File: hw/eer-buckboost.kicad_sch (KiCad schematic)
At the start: 60 parts, among them IC7702 LTC3779IFE#PBF, Q7701 BSC360N15NS3 G, Q7702 BSC360N15NS3 G, Q7703 BSC360N15NS3 G, Q7704 BSC360N15NS3 G, U7751 TLV9062xD, U7752 NVTFS6H888NLTAG, U7753 PCT2075DP

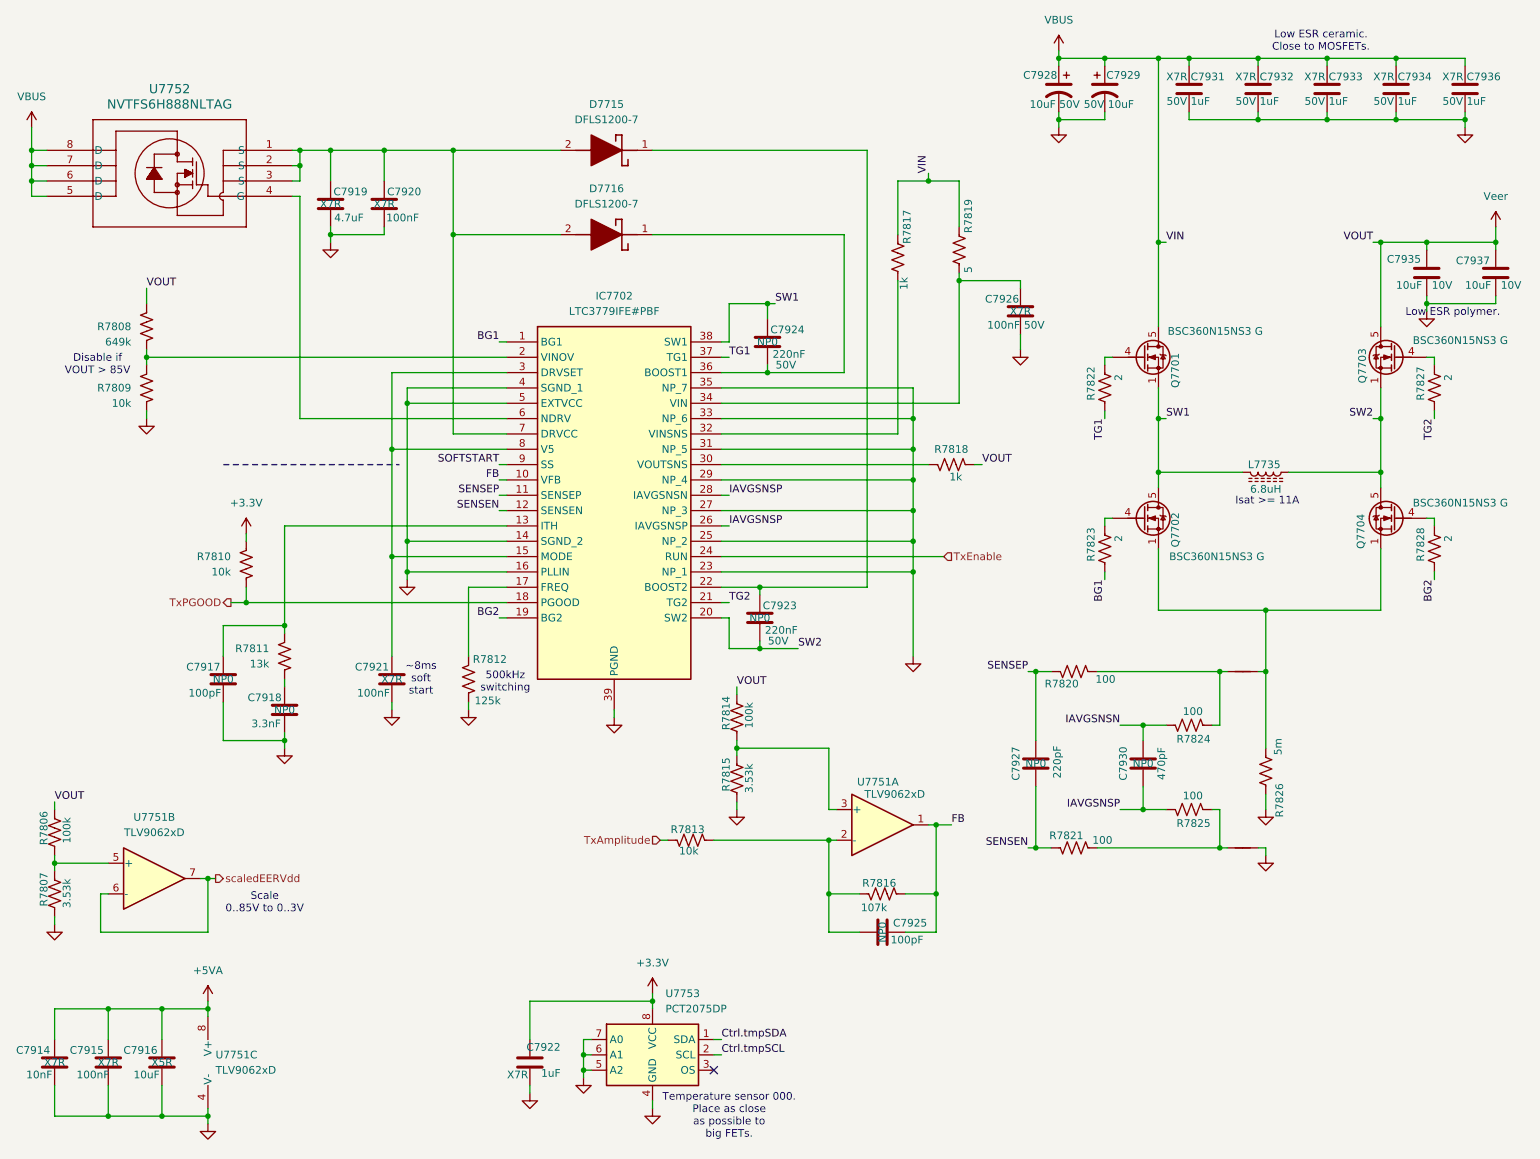
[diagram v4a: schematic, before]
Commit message: Starting to build guanella transformers. Mostly converted to 1-2-1 tx, but FPGA still to do.
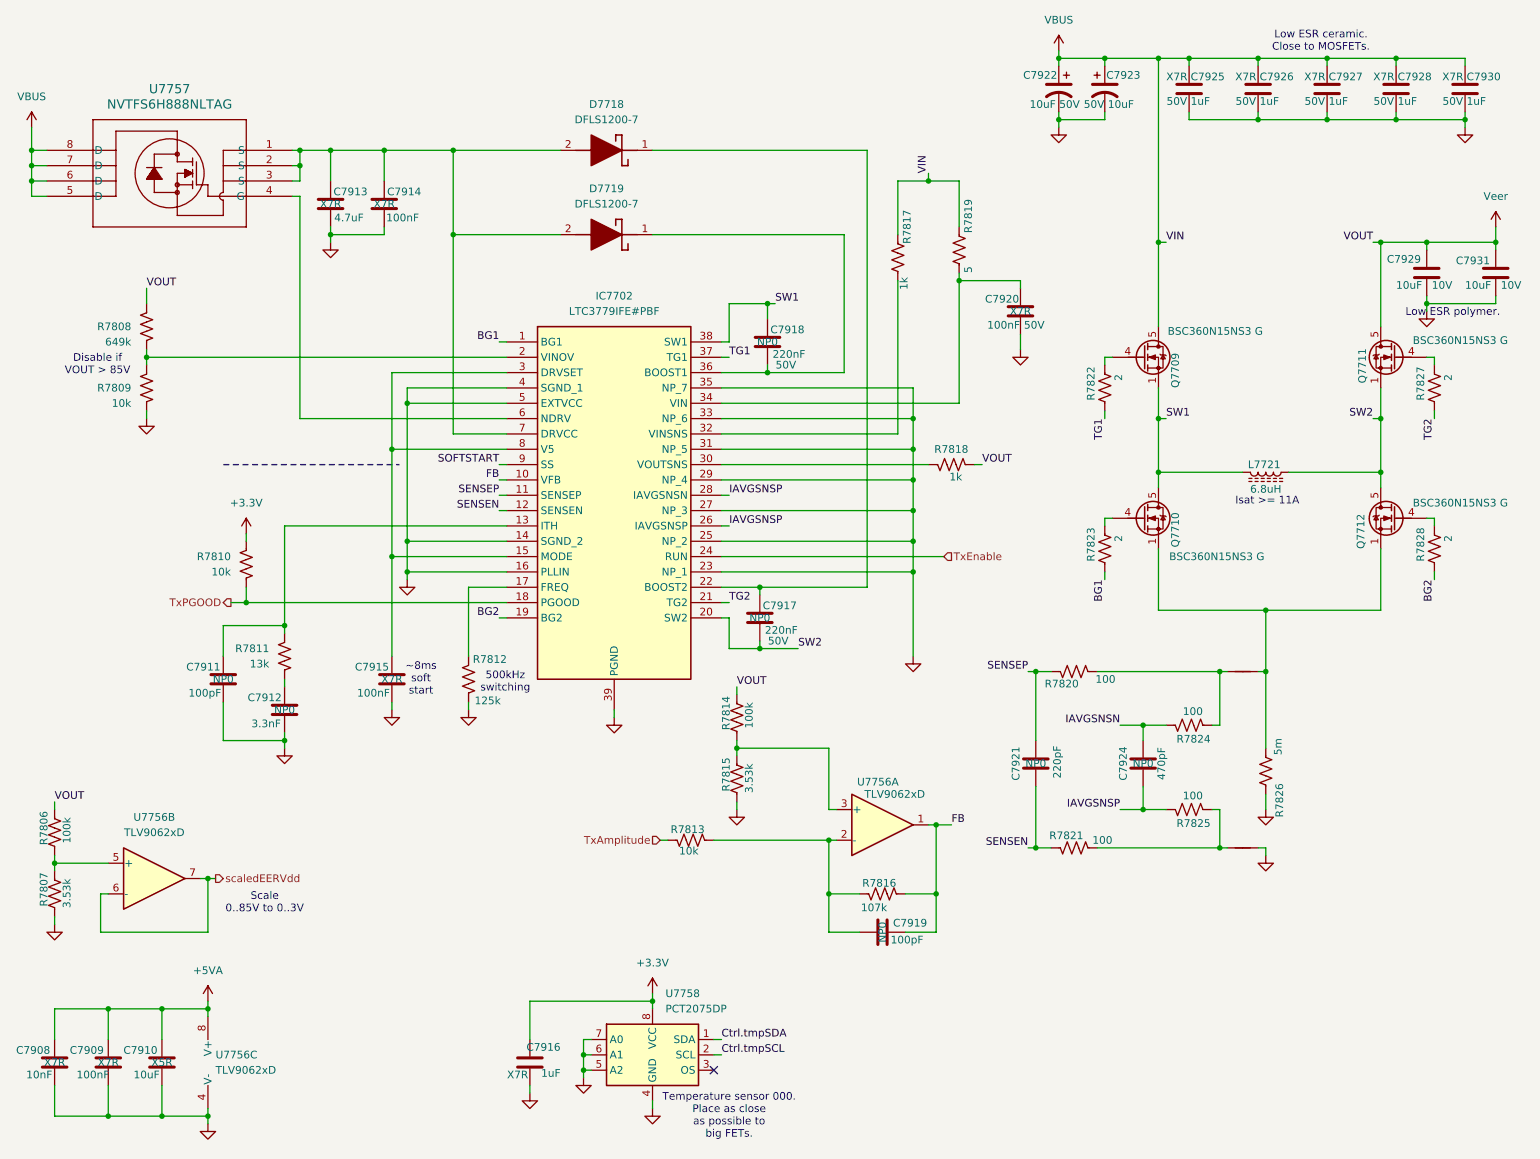
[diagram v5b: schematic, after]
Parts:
- renumbered C7914 to C7908, C7915 to C7909, C7916 to C7910, C7917 to C7911, C7918 to C7912, C7919 to C7913, C7920 to C7914, C7921 to C7915, C7922 to C7916, C7923 to C7917, C7924 to C7918, C7925 to C7919, C7926 to C7920, C7927 to C7921, C7928 to C7922, C7929 to C7923, C7930 to C7924, C7931 to C7925, C7932 to C7926, C7933 to C7927, C7934 to C7928, C7935 to C7929, C7936 to C7930, C7937 to C7931, D7715 to D7718, D7716 to D7719, L7735 to L7721, Q7701 to Q7709, Q7702 to Q7710, Q7703 to Q7711, Q7704 to Q7712, U7751 to U7756, U7752 to U7757, U7753 to U7758

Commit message: Checkpoint. FPGA is mostly done (need a check!). Working on new LPFs. Need inductor footprints and to fix a bunch of broken/missing footprints.
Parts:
- C7908, C7909, C7914, C7915, C7920: footprint Capacitor_SMD:C_0805_2012Metric -> Capacitor_SMD:C_0603_1608Metric
- C7911, C7912, C7919, C7921, C7924: footprint Capacitor_SMD:C_0201_0603Metric -> Capacitor_SMD:C_0603_1608Metric
- R7806, R7809, R7810, R7813, R7814: footprint Resistor_SMD:R_0603_1608Metric -> Resistor_SMD:R_0402_1005Metric
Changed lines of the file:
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@@
 			)
 		)
-		(property "Footprint" "Capacitor_SMD:C_0805_2012Metric"
+		(property "Footprint" "Capacitor_SMD:C_0603_1608Metric"
 			(at 75.2348 49.53 0)
 			(effects
@@
 			)
 		)
-		(property "Footprint" "Capacitor_SMD:C_0805_2012Metric"
+		(property "Footprint" "Capacitor_SMD:C_0603_1608Metric"
 			(at 182.5752 59.69 0)
 			(effects
@@
 			)
 		)
-		(property "Footprint" "Capacitor_SMD:C_0201_0603Metric"
+		(property "Footprint" "Capacitor_SMD:C_0603_1608Metric"
 			(at 50.4952 128.27 0)
 			(effects
@@
 			)
 		)
-		(property "Footprint" "Resistor_SMD:R_0603_1608Metric"
+		(property "Footprint" "Resistor_SMD:R_0402_1005Metric"
 			(at 133.604 130.556 90)
 			(effects
@@
 			)
 		)
-		(property "Footprint" "Resistor_SMD:R_0603_1608Metric"
+		(property "Footprint" "Resistor_SMD:R_0402_1005Metric"
 			(at 52.324 105.664 90)
 			(effects
@@
 			)
 		)
-		(property "Footprint" "Resistor_SMD:R_0603_1608Metric"
+		(property "Footprint" "Resistor_SMD:R_0402_1005Metric"
 			(at 35.814 76.454 90)
 			(effects
@@
 			)
 		)
-		(property "Footprint" "Resistor_SMD:R_0603_1608Metric"
+		(property "Footprint" "Resistor_SMD:R_0402_1005Metric"
 			(at 20.574 149.606 90)
 			(effects
@@
 			)
 		)
-		(property "Footprint" "Capacitor_SMD:C_0805_2012Metric"
+		(property "Footprint" "Capacitor_SMD:C_0603_1608Metric"
 			(at 22.5552 191.77 0)
 			(effects
@@
 			)
 		)
-		(property "Footprint" "Capacitor_SMD:C_0201_0603Metric"
+		(property "Footprint" "Capacitor_SMD:C_0603_1608Metric"
 			(at 60.6552 133.35 0)
 			(effects
@@
 			)
 		)
-		(property "Footprint" "Capacitor_SMD:C_0805_2012Metric"
+		(property "Footprint" "Capacitor_SMD:C_0603_1608Metric"
 			(at 31.4452 191.77 0)
 			(effects
@@
 			)
 		)
-		(property "Footprint" "Resistor_SMD:R_0603_1608Metric"
+		(property "Footprint" "Resistor_SMD:R_0402_1005Metric"
 			(at 127.254 152.146 90)
 			(effects
@@
 			)
 		)
-		(property "Footprint" "Capacitor_SMD:C_0201_0603Metric"
+		(property "Footprint" "Capacitor_SMD:C_0603_1608Metric"
 			(at 202.8952 134.62 0)
 			(effects
@@
 			)
 		)
-		(property "Footprint" "Capacitor_SMD:C_0201_0603Metric"
+		(property "Footprint" "Capacitor_SMD:C_0603_1608Metric"
 			(at 162.56 165.4048 0)
 			(effects
@@
 			)
 		)
-		(property "Footprint" "Capacitor_SMD:C_0201_0603Metric"
+		(property "Footprint" "Capacitor_SMD:C_0603_1608Metric"
 			(at 185.1152 134.62 0)
 			(effects
@@
 			)
 		)
-		(property "Footprint" "Capacitor_SMD:C_0805_2012Metric"
+		(property "Footprint" "Capacitor_SMD:C_0603_1608Metric"
 			(at 78.4352 128.27 0)
 			(effects

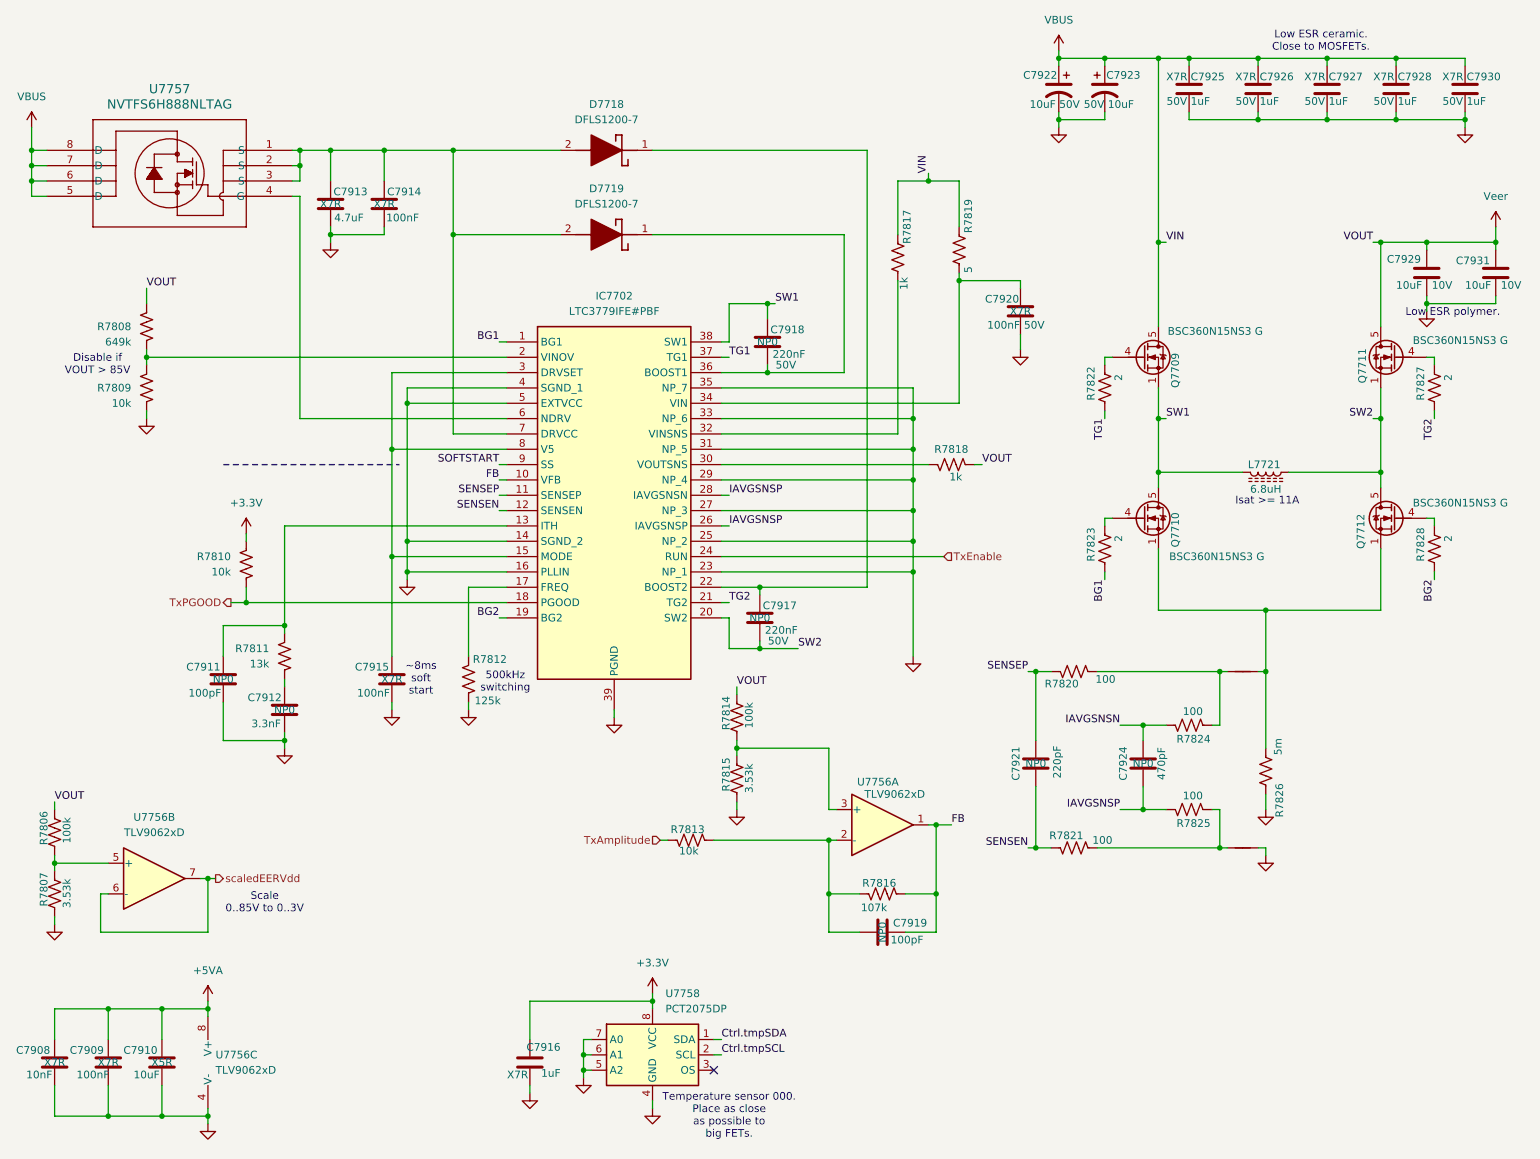
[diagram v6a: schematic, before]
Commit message: OK I have part numbers for consolidated caps, resistors, inductors and all ICs are now Uxxx refdes.
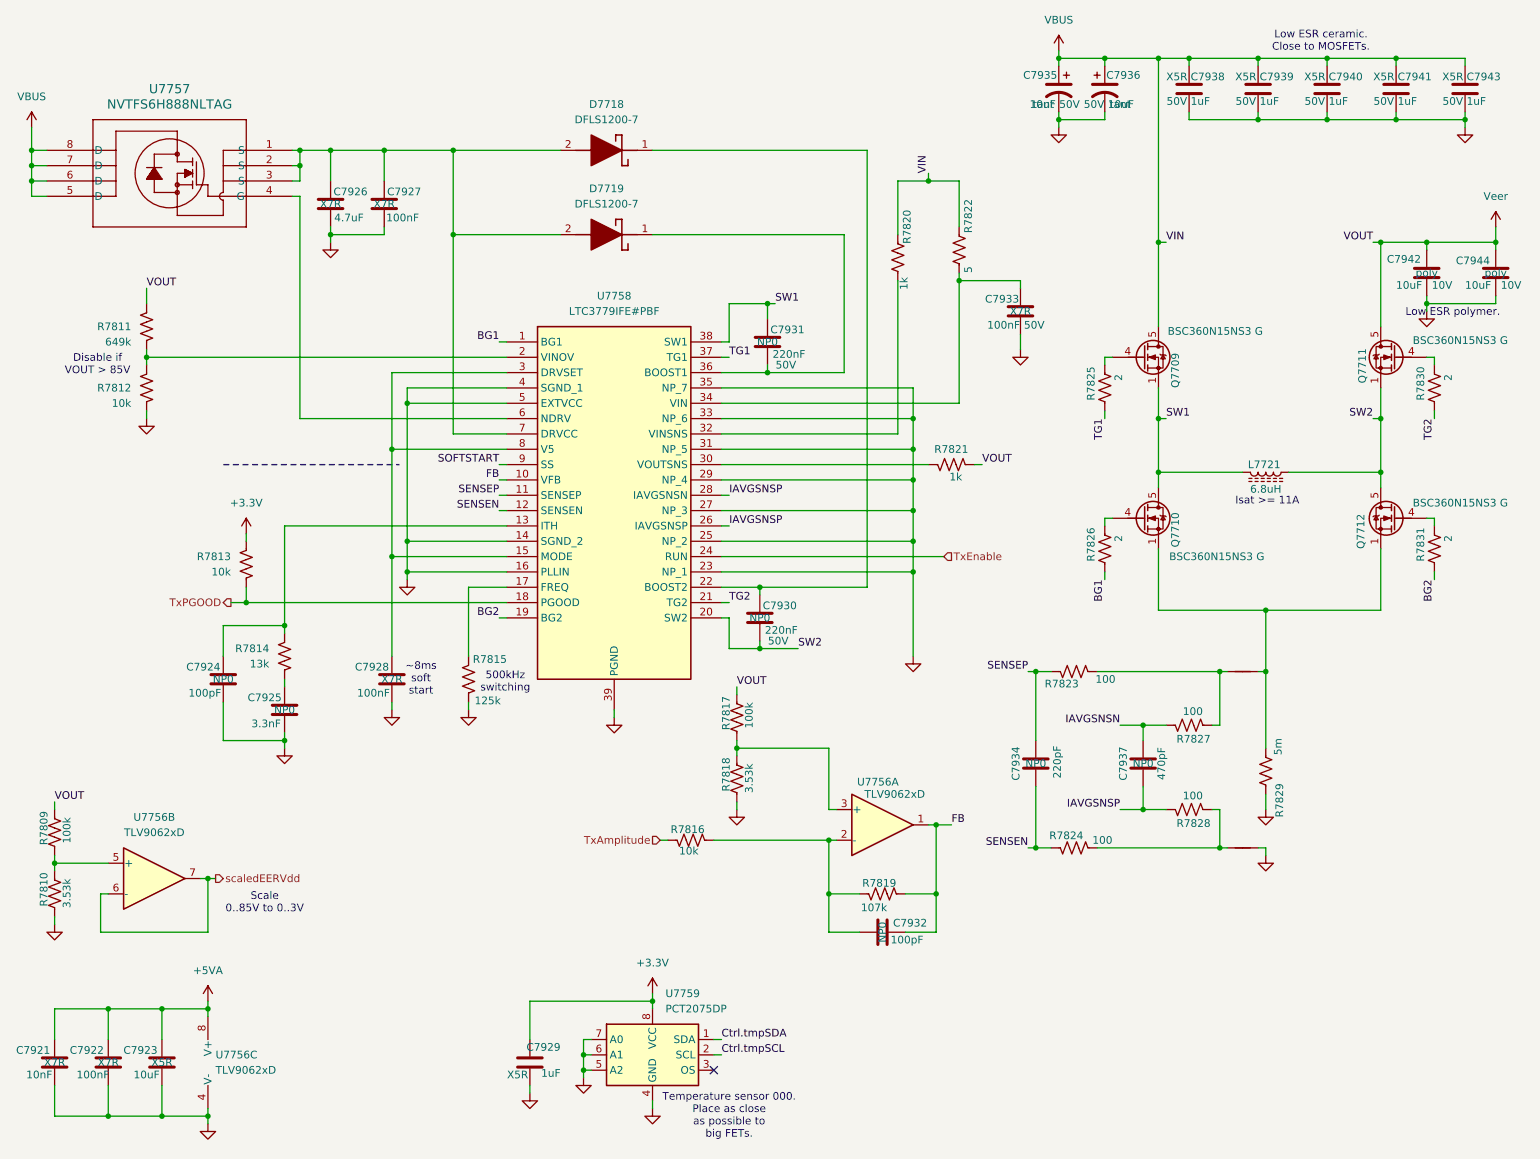
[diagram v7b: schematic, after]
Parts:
- C7921: renamed from C7908; Manufacturer_Name (none) -> Murata; Manufacturer_Part_Number (none) -> GCM1885C2A103JE02J; Mouser Part Number (none) -> 81-GCM1885C2A103JE2J
- C7922: renamed from C7909; Manufacturer_Name (none) -> Kemet; Manufacturer_Part_Number C0603X224J5RACTU -> C0805F104K1RACAUTO; Mouser Part Number 80-C0603X224J5RTU -> 80-C0805F104K1RAUTO
- C7923: renamed from C7910; footprint Capacitor_SMD:C_0805_2012Metric -> Capacitor_SMD:C_0603_1608Metric; Manufacturer_Name (none) -> Taoup Uidem; Manufacturer_Part_Number (none) -> 81-GXT155R71E223KE1D; Mouser Part Number (none) -> 963-MLAST168BB5106MT; working-voltage 10V -> 25V
- C7924: renamed from C7911; Manufacturer_Name (none) -> TDK; Manufacturer_Part_Number (none) -> CGA3E2C0G1H101J080AE; Mouser Part Number (none) -> 810-CGA3E2C0G1H101JA
- C7925: renamed from C7912; Manufacturer_Name (none) -> TDK; Manufacturer_Part_Number (none) -> C1608C0G1H332J080AE; Mouser Part Number (none) -> 810-C1608C0G1H332J08
- C7926: renamed from C7913; Manufacturer_Name (none) -> Kyocera AVX; Manufacturer_Part_Number (none) -> 08055D475KAT4A; Mouser Part Number (none) -> 581-08055D475KAT4A
- C7927: renamed from C7914; Manufacturer_Name (none) -> Kemet; Manufacturer_Part_Number C0603X224J5RACTU -> C0805F104K1RACAUTO; Mouser Part Number 80-C0603X224J5RTU -> 80-C0805F104K1RAUTO
- C7928: renamed from C7915; Manufacturer_Name (none) -> Kemet; Manufacturer_Part_Number C0603X224J5RACTU -> C0805F104K1RACAUTO; Mouser Part Number 80-C0603X224J5RTU -> 80-C0805F104K1RAUTO
- C7929: renamed from C7916; footprint Capacitor_SMD:C_0805_2012Metric -> Capacitor_SMD:C_0402_1005Metric; Manufacturer_Name (none) -> Murata; Manufacturer_Part_Number (none) -> GRM155R61E105KE11D; Mouser Part Number (none) -> 81-GRM155R61E105KE1D; cap-type X7R -> X5R; working-voltage 50V -> 25V
- C7932: renamed from C7919; Manufacturer_Name (none) -> TDK; Manufacturer_Part_Number (none) -> CGA3E2C0G1H101J080AE; Mouser Part Number (none) -> 810-CGA3E2C0G1H101JA
- C7933: renamed from C7920; Manufacturer_Name (none) -> Kemet; Manufacturer_Part_Number C0603X224J5RACTU -> C0805F104K1RACAUTO; Mouser Part Number 80-C0603X224J5RTU -> 80-C0805F104K1RAUTO
- C7934: renamed from C7921; Manufacturer_Name (none) -> TDK; Manufacturer_Part_Number (none) -> C1608C0G1H221F080AA; Mouser Part Number (none) -> 810-C1608C0G1H221F
- C7935: renamed from C7922; footprint CP_Elec_6.3x5.4 -> Capacitor_SMD:C_0805_2012Metric; Manufacturer_Name KEMET -> Kyocera AVX; Manufacturer_Part_Number EXV106M050A9GAA -> TAJD106K050RNJ; Mouser Part Number 80-EXV106M050A9GAA -> 581-TAJD106K050R; cap-type (none) -> tant
- C7936: renamed from C7923; footprint CP_Elec_6.3x5.4 -> Capacitor_SMD:C_0805_2012Metric; Manufacturer_Name KEMET -> Kyocera AVX; Manufacturer_Part_Number EXV106M050A9GAA -> TAJD106K050RNJ; Mouser Part Number 80-EXV106M050A9GAA -> 581-TAJD106K050R; cap-type (none) -> tant
- C7937: renamed from C7924; Manufacturer_Name (none) -> TDK; Manufacturer_Part_Number (none) -> C1608C0G1H471J080AA; Mouser Part Number (none) -> 810-C1608C0G1H471J
- C7938: renamed from C7925; footprint Capacitor_SMD:C_1206_3216Metric -> Capacitor_SMD:C_0603_1608Metric; Manufacturer_Name (none) -> Murata; Manufacturer_Part_Number (none) -> GRM155R61E105KE11D; Mouser Part Number (none) -> 81-GRM155R61E105KE1D; cap-type X7R -> X5R
- C7939: renamed from C7926; footprint Capacitor_SMD:C_1206_3216Metric -> Capacitor_SMD:C_0603_1608Metric; Manufacturer_Name (none) -> Murata; Manufacturer_Part_Number (none) -> GRM155R61E105KE11D; Mouser Part Number (none) -> 81-GRM155R61E105KE1D; cap-type X7R -> X5R
- C7940: renamed from C7927; footprint Capacitor_SMD:C_1206_3216Metric -> Capacitor_SMD:C_0603_1608Metric; Manufacturer_Name (none) -> Murata; Manufacturer_Part_Number (none) -> GRM155R61E105KE11D; Mouser Part Number (none) -> 81-GRM155R61E105KE1D; cap-type X7R -> X5R
- C7941: renamed from C7928; footprint Capacitor_SMD:C_1206_3216Metric -> Capacitor_SMD:C_0603_1608Metric; Manufacturer_Name (none) -> Murata; Manufacturer_Part_Number (none) -> GRM155R61E105KE11D; Mouser Part Number (none) -> 81-GRM155R61E105KE1D; cap-type X7R -> X5R
- C7942: renamed from C7929; cap-type (none) -> poly
- C7943: renamed from C7930; footprint Capacitor_SMD:C_1206_3216Metric -> Capacitor_SMD:C_0603_1608Metric; Manufacturer_Name (none) -> Murata; Manufacturer_Part_Number (none) -> GRM155R61E105KE11D; Mouser Part Number (none) -> 81-GRM155R61E105KE1D; cap-type X7R -> X5R
- C7944: renamed from C7931; cap-type (none) -> poly
- renumbered C7917 to C7930, C7918 to C7931, R7806 to R7809, R7807 to R7810, R7808 to R7811, R7809 to R7812, R7810 to R7813, R7811 to R7814, R7812 to R7815, R7813 to R7816, R7814 to R7817, R7815 to R7818, R7816 to R7819, R7817 to R7820, R7818 to R7821, R7819 to R7822, R7820 to R7823, R7821 to R7824, R7822 to R7825, R7823 to R7826, R7824 to R7827, R7825 to R7828, R7826 to R7829, R7827 to R7830, R7828 to R7831, IC7702 to U7758, U7758 to U7759
